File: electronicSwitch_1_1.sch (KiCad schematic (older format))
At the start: 16 parts, among them P6 JUMPER3, Q1 SI2369, Q2 TSM2314, Q3 SI2369

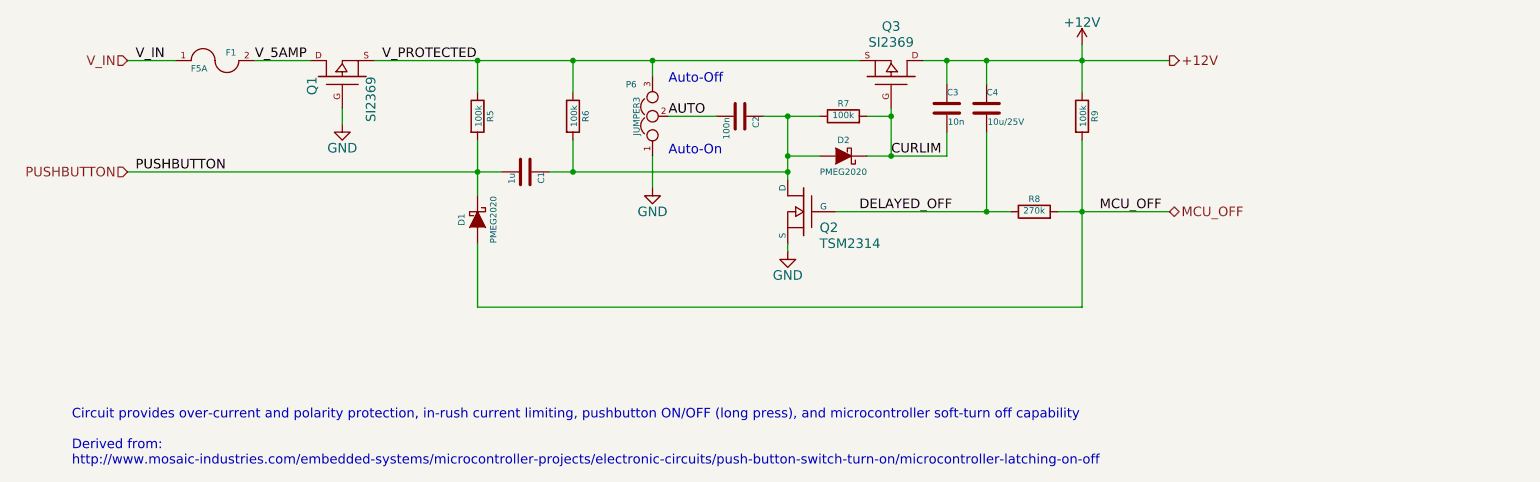
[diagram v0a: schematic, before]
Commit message: Added load resistor. Changed part references in consequence.
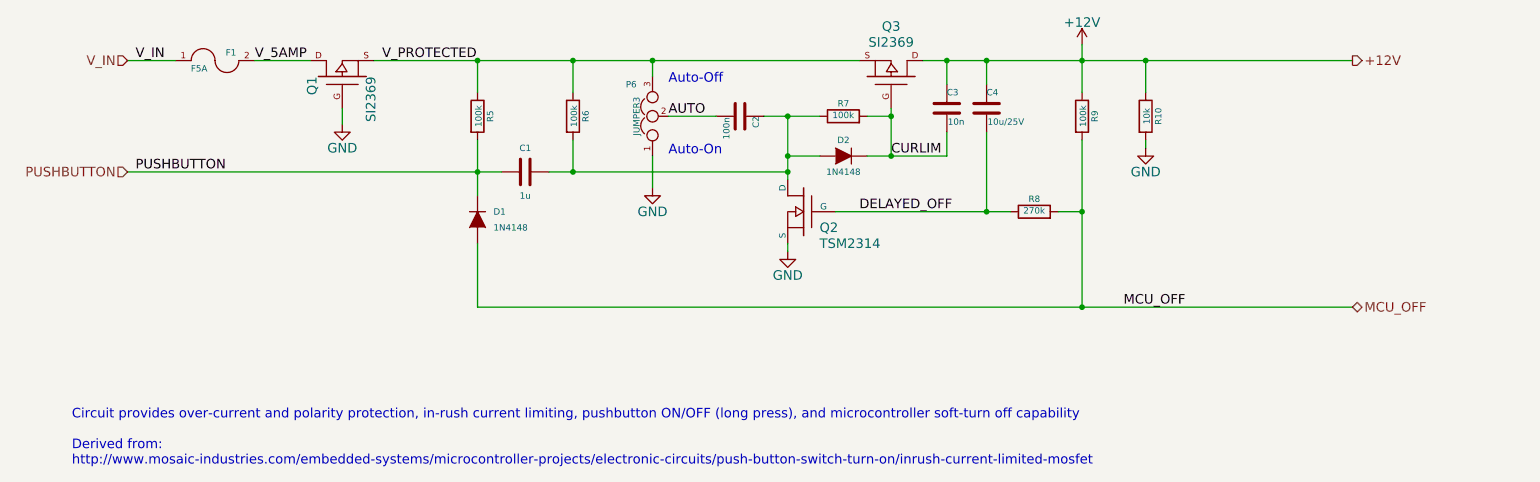
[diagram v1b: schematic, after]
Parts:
- removed D1, D2: PMEG2020, Diodes_SMD:SOD-323, symbol D_Schottky
- added D1, D2: 1N4148, Diodes_SMD:SOD-323, symbol D
- added R10: 10k, Resistors_SMD:R_0805, symbol R
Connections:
- net +12V: now also R10.1
- net CURLIM: now also D2.1 (K)
- net GND: now also R10.2
- net MCU_OFF: now also D1.2 (A)
- net PUSHBUTTON: now also D1.1 (K)
- net at C1.1, C2.1, Q2.D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: now also D2.2 (A)
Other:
- note added: "Circuit provides over-current and polarity protection, in-rush current limiting, pushbutton ON/OFF (long press), and microcontroller soft-turn off capability\n\nDerived from:\nhttp://www.mosaic-industries.com/embedded-systems/microcontroller-projects/electronic-circuits/push-button-switch-turn-on/inrush-current-limited-mosfet"
- note removed: "Circuit provides over-current and polarity protection, in-rush current limiting, pushbutton ON/OFF (long press), and microcontroller soft-turn off capability\n\nDerived from:\nhttp://www.mosaic-industries.com/embedded-systems/microcontroller-projects/electronic-circuits/push-button-switch-turn-on/microcontroller-latching-on-off"
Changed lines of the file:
@@
 AR Path="/54DADBD1" Ref="C1"  Part="1"
 AR Path="/54DAD8AC/54DADBD1" Ref="C1"  Part="1"
-F 0 "C1" H 4800 3250 40  0000 L CNN
-F 1 "1u" H 4806 3065 40  0000 L CNN
+F 0 "C1" V 4650 3150 40  0000 C CNN
+F 1 "1u" V 4950 3150 40  0000 C CNN
 F 2 "Capacitors_SMD:C_0805" H 4838 3000 30  0001 C CNN
 F 3 "" H 4800 3150 60  0000 C CNN
@@
 Connection ~ 7100 3050
 Wire Wire Line
-	7300 2450 8850 2450
+	7300 2450 10000 2450
 Wire Wire Line
 	7450 2450 7450 2600
@@
 	4500 3600 4500 4000
 Wire Wire Line
-	4500 4000 8300 4000
-Wire Wire Line
-	8300 4000 8300 2950
-Wire Wire Line
-	8150 3400 8850 3400
+	4500 4000 10000 4000
+Wire Wire Line
+	8300 2950 8300 4000
+Wire Wire Line
+	8150 3400 8300 3400
 Connection ~ 8300 3400
 $Comp
@@
 V_IN
 Connection ~ 8300 2450
-Text Label 8800 3400 2    60   ~ 0
+Text Label 8950 4000 2    60   ~ 0
 MCU_OFF
 Text HLabel 2300 2450 0    60   Input ~ 0
@@
 Text HLabel 2300 3150 0    60   Input ~ 0
 PUSHBUTTON
-Text HLabel 8850 3400 2    60   BiDi ~ 0
+Text HLabel 10000 4000 2    60   BiDi ~ 0
 MCU_OFF
 Text Notes 5700 2600 0    60   ~ 0
@@
 $EndComp
 Text Notes 1950 5000 0    60   ~ 0
-Circuit provides over-current and polarity protection, in-rush current limiting, pushbutton ON/OFF (long press), and microcontroller soft-turn off capability\n\nDerived from:\nhttp://www.mosaic-industries.com/embedded-systems/microcontroller-projects/electronic-circuits/push-button-switch-turn-on/microcontroller-latching-on-off
-Text HLabel 8850 2450 2    60   Output ~ 0
+Circuit provides over-current and polarity protection, in-rush current limiting, pushbutton ON/OFF (long press), and microcontroller soft-turn off capability\n\nDerived from:\nhttp://www.mosaic-industries.com/embedded-systems/microcontroller-projects/electronic-circuits/push-button-switch-turn-on/inrush-current-limited-mosfet
+Text HLabel 10000 2450 2    60   Output ~ 0
 +12V
 Wire Wire Line
@@
 $EndComp
 $Comp
-L D_Schottky D1
-U 1 1 569070E8
+L D D2
+U 1 1 569E6D02
+P 6800 3050
+F 0 "D2" H 6800 2950 40  0000 C CNN
+F 1 "1N4148" H 6800 3150 40  0000 C CNN
+F 2 "Diodes_SMD:SOD-323" H 6800 3050 50  0001 C CNN
+F 3 "" H 6800 3050 50  0000 C CNN
+F 4 "1N4148WS" H 6800 3050 60  0001 C CNN "Part Number"
+F 5 "Multicomp" H 6800 3050 60  0001 C CNN "Manufacturer"
+F 6 "1466524" H 6800 3050 60  0001 C CNN "Field6"
+	1    6800 3050
+	-1   0    0    1
+$EndComp
+$Comp
+L D D1
+U 1 1 569E7C5B
 P 4500 3450
-F 0 "D1" H 4500 3350 40  0000 C CNN
-F 1 "PMEG2020" H 4500 3550 40  0000 C CNN
+F 0 "D1" V 4450 3550 40  0000 L CNN
+F 1 "1N4148" V 4550 3550 40  0000 L CNN
 F 2 "Diodes_SMD:SOD-323" H 4500 3450 50  0001 C CNN
 F 3 "" H 4500 3450 50  0000 C CNN
-F 4 "PMEG2020AEA" H 4500 3450 60  0001 C CNN "Part Number"
-F 5 "NXP Semiconductors" H 4500 3450 60  0001 C CNN "Manufacturer"
-F 6 "8737940" H 4500 3450 60  0001 C CNN "Order Code"
+F 4 "1N4148WS" H 4500 3450 60  0001 C CNN "Part Number"
+F 5 "Multicomp" H 4500 3450 60  0001 C CNN "Manufacturer"
+F 6 "1466524" H 4500 3450 60  0001 C CNN "Field6"
 	1    4500 3450
 	0    1    1    0
 $EndComp
 $Comp
-L D_Schottky D2
-U 1 1 56907922
-P 6800 3050
-F 0 "D2" H 6800 2950 40  0000 C CNN
-F 1 "PMEG2020" H 6800 3150 40  0000 C CNN
-F 2 "Diodes_SMD:SOD-323" H 6800 3050 50  0001 C CNN
-F 3 "" H 6800 3050 50  0000 C CNN
-F 4 "PMEG2020AEA" H 6800 3050 60  0001 C CNN "Part Number"
-F 5 "NXP Semiconductors" H 6800 3050 60  0001 C CNN "Manufacturer"
-F 6 "8737940" H 6800 3050 60  0001 C CNN "Order Code"
-	1    6800 3050
-	-1   0    0    1
-$EndComp
+L R R10
+U 1 1 569E9A51
+P 8700 2800
+F 0 "R10" V 8780 2800 40  0000 C CNN
+F 1 "10k" V 8707 2801 40  0000 C CNN
+F 2 "Resistors_SMD:R_0805" V 8630 2800 30  0001 C CNN
+F 3 "" H 8700 2800 30  0000 C CNN
+F 4 "MCMR08X1002FTL" V 8700 2800 60  0001 C CNN "Part Number"
+F 5 "Multicomp" V 8700 2800 60  0001 C CNN "Manufacturer"
+F 6 "2073607" V 8700 2800 60  0001 C CNN "Order Code"
+	1    8700 2800
+	1    0    0    -1
+$EndComp
+Wire Wire Line
+	8700 2950 8700 3000
+$Comp
+L GND #PWR033
+U 1 1 569E9A8F
+P 8700 3000
+F 0 "#PWR033" H 8700 2750 60  0001 C CNN
+F 1 "GND" H 8700 2850 60  0000 C CNN
+F 2 "" H 8700 3000 60  0000 C CNN
+F 3 "" H 8700 3000 60  0000 C CNN
+	1    8700 3000
+	1    0    0    -1
+$EndComp
+Wire Wire Line
+	8700 2650 8700 2450
+Connection ~ 8700 2450
+Connection ~ 8300 4000
 $EndSCHEMATC

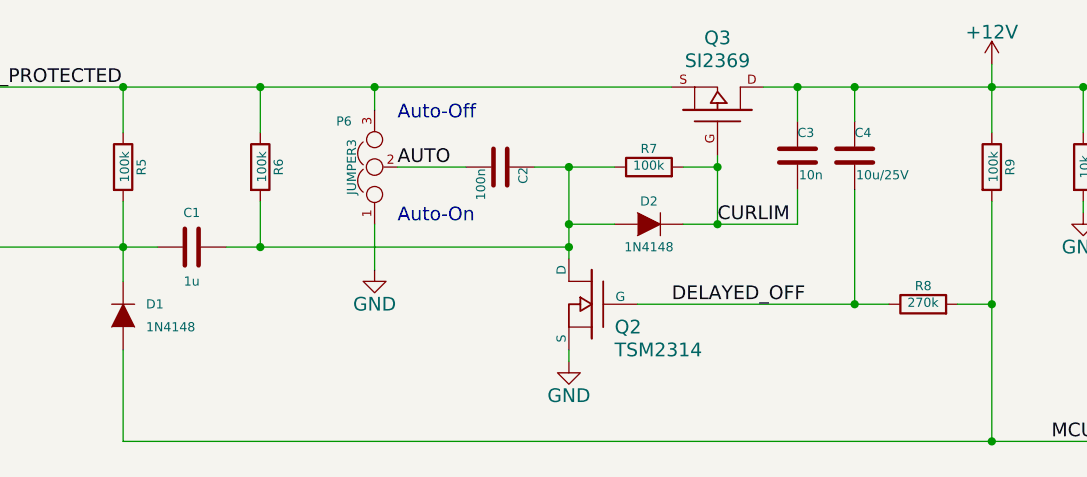
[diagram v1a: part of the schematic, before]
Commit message: Added detailed part descriptions
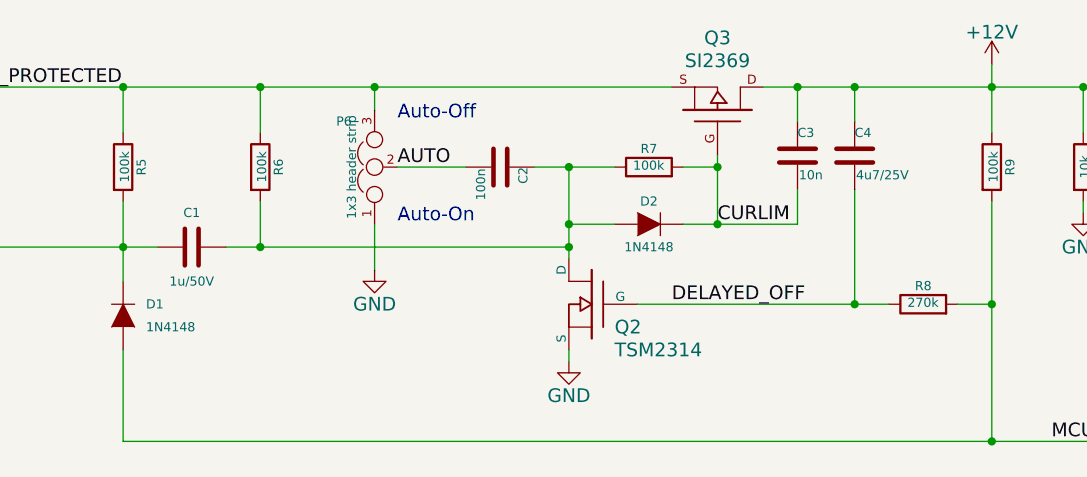
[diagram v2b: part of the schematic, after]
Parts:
- C1: value 1u -> 1u/50V; Alt. Order Code (none) -> 81-GRM219R61H105KA3D; Alt. Supplier (none) -> Mouser; Note (none) -> 1μF/50V X5R 0805 ceramic capacitor; Package (none) -> 0805; Supplier (none) -> Farnell
- C2: Alt. Order Code (none) -> 710-885012207098; Alt. Supplier (none) -> Mouser; Note (none) -> 100nF/50V X7R 0805 ceramic capacitor; Package (none) -> 0805; Supplier (none) -> Farnell
- C3: Alt. Order Code (none) -> 710-885012207092; Alt. Supplier (none) -> Mouser; Note (none) -> 10nF/50V X7R 0805 ceramic capacitor; Package (none) -> 0805; Supplier (none) -> Farnell
- C4: value 10u/25V -> 4u7/25V; Alt. Order Code (none) -> 81-GRM21BR61E475MA2L; Alt. Supplier (none) -> Mouser; Note (none) -> 4.7μF/25V X5R 0805 ceramic capacitor; Order Code 2426961 -> 2362111; Package (none) -> 0805; Part Number GRM219R61E106KA12D -> GRM21BR61E475MA12L; Supplier (none) -> Farnell
- D1, D2: Alt. Order Code (none) -> 512-1N4148WS; Alt. Supplier (none) -> Mouser; Field6 1466524 -> (none); Note (none) -> Small signal SOD-323 diode; Order Code (none) -> 1466524; Package (none) -> SOD-323; Supplier (none) -> Farnell
- F1: Alt. Order Code (none) -> 530-C1Q5; Alt. Supplier (none) -> Mouser; Note (none) -> Fast blow 5 A fuse; Package (none) -> 1206; Supplier (none) -> Farnell
- P6: value JUMPER3 -> 1x3 header strip; Alt. Order Code (none) -> 855-M20-9990346; Alt. Supplier (none) -> Mouser; Note (none) -> 2-way jumper switch; Package (none) -> SIL-3; Supplier (none) -> Farnell
- Q1: Alt. Order Code (none) -> 78-SI2369DS-T1-GE3; Alt. Supplier (none) -> Mouser; Note (none) -> P-channel SOT-23 MOSFET; Package (none) -> SOT-23; Supplier (none) -> Farnell
- Q2: Alt. Order Code (none) -> 781-SI2314EDS-E3; Alt. Supplier (none) -> Mouser; Note (none) -> N-channel SOT-23 MOSFET; Package (none) -> SOT-23; Supplier (none) -> Farnell
- Q3: Alt. Order Code (none) -> 781-SI2314EDS-E3; Alt. Supplier (none) -> Mouser; Note (none) -> P-channel SOT-23 MOSFET; Package (none) -> SOT-23; Supplier (none) -> Farnell
- R10: Alt. Order Code (none) -> 71-CRCW0805-10K-E3; Alt. Supplier (none) -> Mouser; Note (none) -> 10kΩ/1% 0805 resistor; Package (none) -> 0805; Supplier (none) -> Farnell
- R5, R6, R7, R9: Alt. Order Code (none) -> 71-CRCW0805-100K-E3; Alt. Supplier (none) -> Mouser; Note (none) -> 100kΩ/1% 0805 resistor; Package (none) -> 0805; Supplier (none) -> Farnell
- R8: Alt. Order Code (none) -> ERJ-6ENF2703V; Alt. Supplier (none) -> Mouser; Note (none) -> 270kΩ/1% 0805 resistor; Package (none) -> 0805; Supplier (none) -> Farnell
